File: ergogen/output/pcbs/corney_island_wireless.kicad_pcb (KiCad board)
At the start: 2 copper layers, 133.8 x 91.7 mm, 75 parts

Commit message: Update assets
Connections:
- MCU1 pad 1: LED -> MCU1_1
- MCU1 pad 10: R2 -> MCU1_10
- MCU1 pad 11: R3 -> MCU1_11
- MCU1 pad 12: P9 -> MCU1_12
- MCU1 pad 2: DAT -> MCU1_2
- MCU1 pad 3: GND -> MCU1_3
- MCU1 pad 4: GND -> MCU1_4
- MCU1 pad 5: SDA -> MCU1_5
- MCU1 pad 6: SCL -> MCU1_6
- MCU1 pad 7: CS -> MCU1_7
- MCU1 pad 8: R0 -> MCU1_8
- MCU1 pad 9: R1 -> MCU1_9
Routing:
- net index_top: track 101.6 -> 0.00 mm
- net outer_bottom: track 101.4 -> 0.00 mm
- net inner_top: track 50.9 -> 0.00 mm
- net inner_home: track 50.9 -> 0.00 mm
- net GND: track 3.50 -> 28.9 mm
- net C1: track 0.00 -> 9.64 mm
- net VCC: track 0.00 -> 9.64 mm
- net RST: track 0.00 -> 9.64 mm
- net RAW: track 0.00 -> 9.64 mm
- net P16: track 0.00 -> 9.64 mm
- net P10: track 0.00 -> 9.64 mm
- net C5: track 0.00 -> 9.64 mm
- net C4: track 0.00 -> 9.64 mm
- net C2: track 0.00 -> 9.64 mm
- net R3: track 0.00 -> 9.63 mm
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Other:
- outline, holes or cut-outs redrawn
- net class Default removed

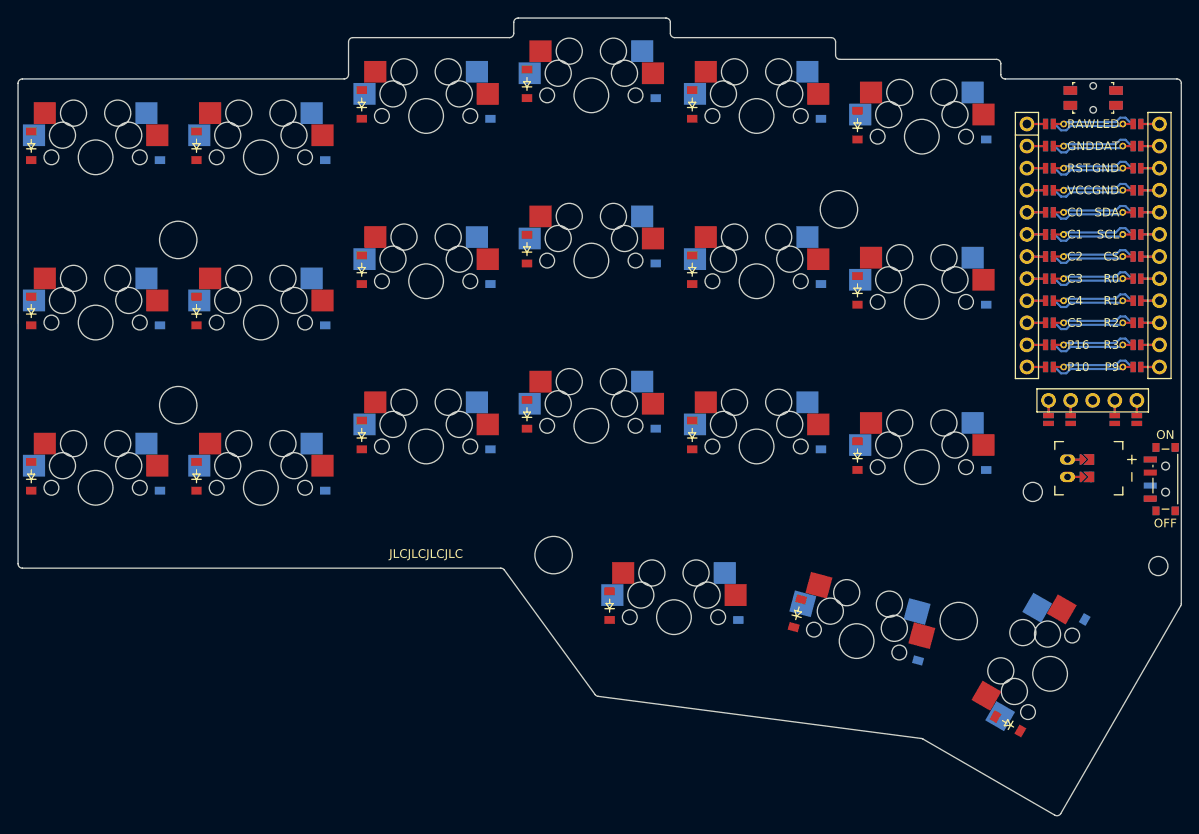
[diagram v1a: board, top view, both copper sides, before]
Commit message: Switch to KiCad 8 PCB template and require Ergogen v4.1.0
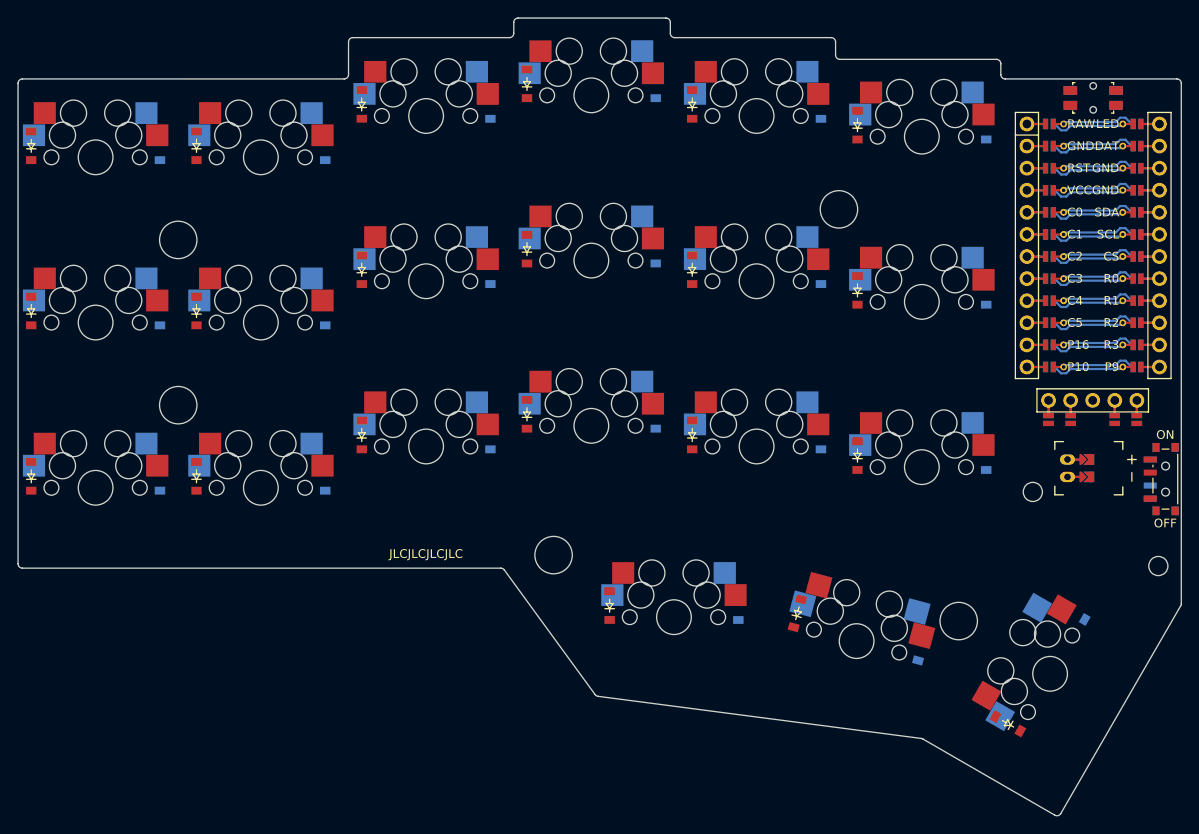
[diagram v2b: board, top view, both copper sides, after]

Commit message: Update assets
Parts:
- added S22: , ceoloide:switch_mx, F.Cu at (100.0, 100.0)
- added S23: , ceoloide:switch_mx, F.Cu at (100.0, 81.0)
- added S24: , ceoloide:switch_mx, F.Cu at (100.0, 62.0)
- added S25: , ceoloide:switch_mx, F.Cu at (119.0, 100.0)
- added S26: , ceoloide:switch_mx, F.Cu at (119.0, 81.0)
- added S27: , ceoloide:switch_mx, F.Cu at (119.0, 62.0)
- added S28: , ceoloide:switch_mx, F.Cu at (138.0, 95.2)
- added S29: , ceoloide:switch_mx, F.Cu at (138.0, 76.2)
- added S30: , ceoloide:switch_mx, F.Cu at (138.0, 57.2)
- added S31: , ceoloide:switch_mx, F.Cu at (157.0, 92.9)
- added S32: , ceoloide:switch_mx, F.Cu at (157.0, 73.9)
- added S33: , ceoloide:switch_mx, F.Cu at (157.0, 54.9)
- added S34: , ceoloide:switch_mx, F.Cu at (176.0, 95.2)
- added S35: , ceoloide:switch_mx, F.Cu at (176.0, 76.2)
- added S36: , ceoloide:switch_mx, F.Cu at (176.0, 57.2)
- added S37: , ceoloide:switch_mx, F.Cu at (195.0, 97.6)
- added S38: , ceoloide:switch_mx, F.Cu at (195.0, 78.6)
- added S39: , ceoloide:switch_mx, F.Cu at (195.0, 59.6)
- added S40: , ceoloide:switch_mx, F.Cu at (166.5, 114.9)
- added S41: , ceoloide:switch_mx, F.Cu at (187.5, 117.6)
- added S42: , ceoloide:switch_mx, F.Cu at (209.7, 121.4)
- PWR1: value power_switch -> (none)
- RST1: value reset_button_smd_side -> (none); footprint ceoloide:reset_button_smd_side -> ceoloide:reset_switch_smd_side
- S1, S10, S11, S12, S13, S14, S15, S16, S17, S18, S19, S2, S20, S21, S3, S4, S5, S6, S7, S8, S9: footprint MX -> ceoloide:switch_mx; moved to B.Cu
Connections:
- D1 pad 2: outer_bottom -> outer_bottom_B
- D10 pad 2: middle_bottom -> middle_bottom_B
- D11 pad 2: middle_home -> middle_home_B
- D12 pad 2: middle_top -> middle_top_B
- D13 pad 2: index_bottom -> index_bottom_B
- D14 pad 2: index_home -> index_home_B
- D15 pad 2: index_top -> index_top_B
- D16 pad 2: inner_bottom -> inner_bottom_B
- D17 pad 2: inner_home -> inner_home_B
- D18 pad 2: inner_top -> inner_top_B
- D19 pad 2: near_home -> near_home_B
- D2 pad 2: outer_home -> outer_home_B
- D20 pad 2: mid_home -> mid_home_B
- D21 pad 2: far_home -> far_home_B
- D22 pad 2: outer_bottom -> outer_bottom_F
- D23 pad 2: outer_home -> outer_home_F
- D24 pad 2: outer_top -> outer_top_F
- D25 pad 2: pinky_bottom -> pinky_bottom_F
- D26 pad 2: pinky_home -> pinky_home_F
- D27 pad 2: pinky_top -> pinky_top_F
- D28 pad 2: ring_bottom -> ring_bottom_F
- D29 pad 2: ring_home -> ring_home_F
- D3 pad 2: outer_top -> outer_top_B
- D30 pad 2: ring_top -> ring_top_F
- D31 pad 2: middle_bottom -> middle_bottom_F
- D32 pad 2: middle_home -> middle_home_F
- D33 pad 2: middle_top -> middle_top_F
- D34 pad 2: index_bottom -> index_bottom_F
- D35 pad 2: index_home -> index_home_F
- D36 pad 2: index_top -> index_top_F
- D37 pad 2: inner_bottom -> inner_bottom_F
- D38 pad 2: inner_home -> inner_home_F
- D39 pad 2: inner_top -> inner_top_F
- D4 pad 2: pinky_bottom -> pinky_bottom_B
- D40 pad 2: near_home -> near_home_F
- D41 pad 2: mid_home -> mid_home_F
- D42 pad 2: far_home -> far_home_F
- D5 pad 2: pinky_home -> pinky_home_B
- D6 pad 2: pinky_top -> pinky_top_B
- D7 pad 2: ring_bottom -> ring_bottom_B
- D8 pad 2: ring_home -> ring_home_B
- D9 pad 2: ring_top -> ring_top_B
- MCU1 pad 1: MCU1_1 -> RAW
- MCU1 pad 10: MCU1_10 -> C5
- MCU1 pad 11: MCU1_11 -> P16
- MCU1 pad 12: MCU1_12 -> P10
- MCU1 pad 13: MCU1_12 -> P9
- MCU1 pad 14: MCU1_11 -> R3
- MCU1 pad 15: MCU1_10 -> R2
- MCU1 pad 16: MCU1_9 -> R1
- MCU1 pad 17: MCU1_8 -> R0
- MCU1 pad 18: MCU1_7 -> CS
- MCU1 pad 19: MCU1_6 -> SCL
- MCU1 pad 2: MCU1_2 -> GND
- MCU1 pad 20: MCU1_5 -> SDA
- MCU1 pad 21: MCU1_4 -> GND
- MCU1 pad 22: MCU1_3 -> GND
- MCU1 pad 23: MCU1_2 -> DAT
- MCU1 pad 24: MCU1_1 -> LED
- MCU1 pad 3: MCU1_3 -> RST
- MCU1 pad 4: MCU1_4 -> VCC
- MCU1 pad 5: MCU1_5 -> C0
- MCU1 pad 6: MCU1_6 -> C1
- MCU1 pad 7: MCU1_7 -> C2
- MCU1 pad 8: MCU1_8 -> C3
- MCU1 pad 9: MCU1_9 -> C4
- S1 pad 2: outer_bottom -> outer_bottom_B
- S10 pad 2: middle_bottom -> middle_bottom_B
- S11 pad 2: middle_home -> middle_home_B
- S12 pad 2: middle_top -> middle_top_B
- S13 pad 2: index_bottom -> index_bottom_B
- S14 pad 2: index_home -> index_home_B
- S15 pad 2: index_top -> index_top_B
- S16 pad 2: inner_bottom -> inner_bottom_B
- S17 pad 2: inner_home -> inner_home_B
- S18 pad 2: inner_top -> inner_top_B
- S19 pad 2: near_home -> near_home_B
- S2 pad 2: outer_home -> outer_home_B
- S20 pad 2: mid_home -> mid_home_B
- S21 pad 2: far_home -> far_home_B
- S3 pad 2: outer_top -> outer_top_B
- S4 pad 2: pinky_bottom -> pinky_bottom_B
- S5 pad 2: pinky_home -> pinky_home_B
- S6 pad 2: pinky_top -> pinky_top_B
- S7 pad 2: ring_bottom -> ring_bottom_B
- S8 pad 2: ring_home -> ring_home_B
- S9 pad 2: ring_top -> ring_top_B
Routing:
- net GND: track 28.9 -> 0.00 mm
- net C3: track 9.64 -> 0.00 mm
- net C1: track 9.64 -> 0.00 mm
- net VCC: track 9.64 -> 0.00 mm
- net RST: track 9.64 -> 0.00 mm
- net RAW: track 9.64 -> 0.00 mm
- net C4: track 9.64 -> 0.00 mm
- net C2: track 9.64 -> 0.00 mm
- net C0: track 9.64 -> 0.00 mm
- net P16: track 9.64 -> 0.00 mm
- net P10: track 9.64 -> 0.00 mm
- net C5: track 9.64 -> 0.00 mm
- net SDA: track 9.63 -> 0.00 mm
- net R3: track 9.63 -> 0.00 mm
- net R1: track 9.63 -> 0.00 mm
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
